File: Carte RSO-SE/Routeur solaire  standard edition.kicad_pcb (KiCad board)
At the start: 2 copper layers, 103.5 x 174.1 mm, 48 parts

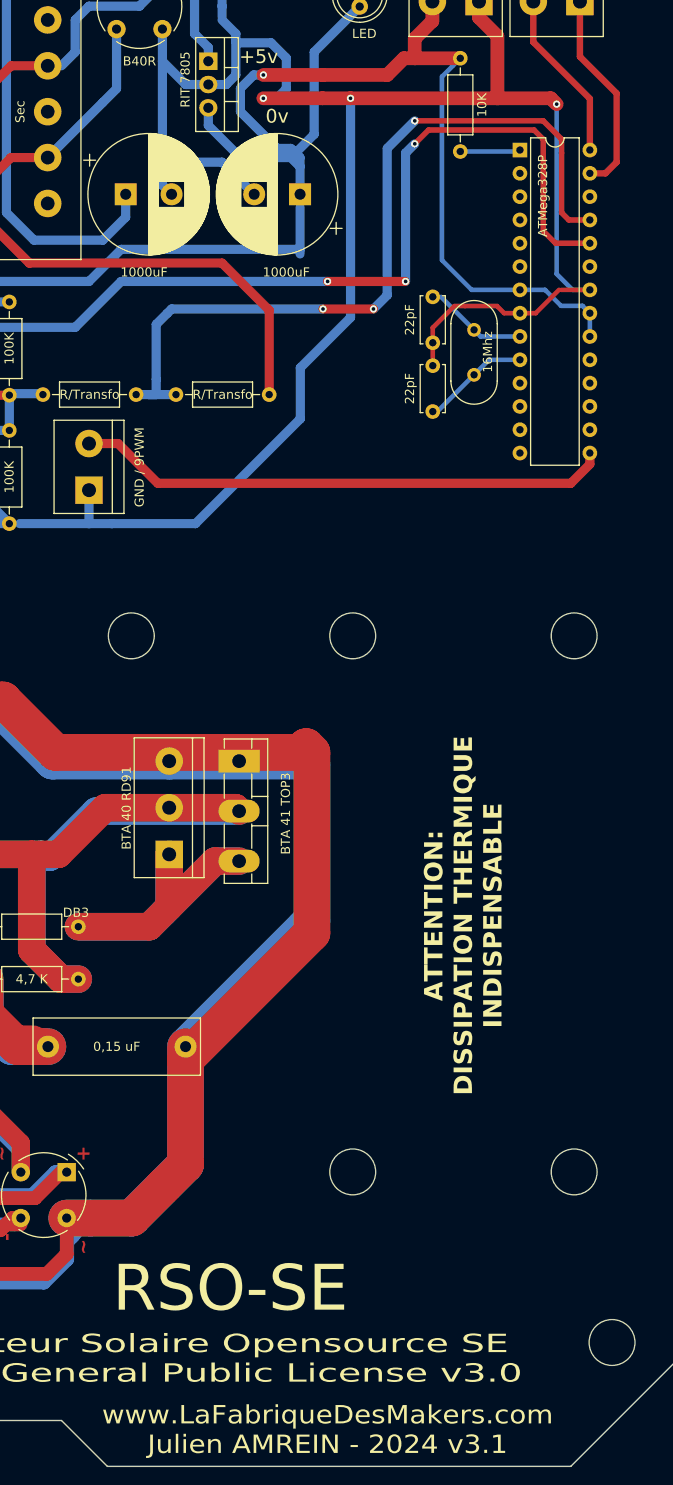
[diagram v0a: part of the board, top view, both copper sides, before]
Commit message: Ajout prise pour sonde de température en A3
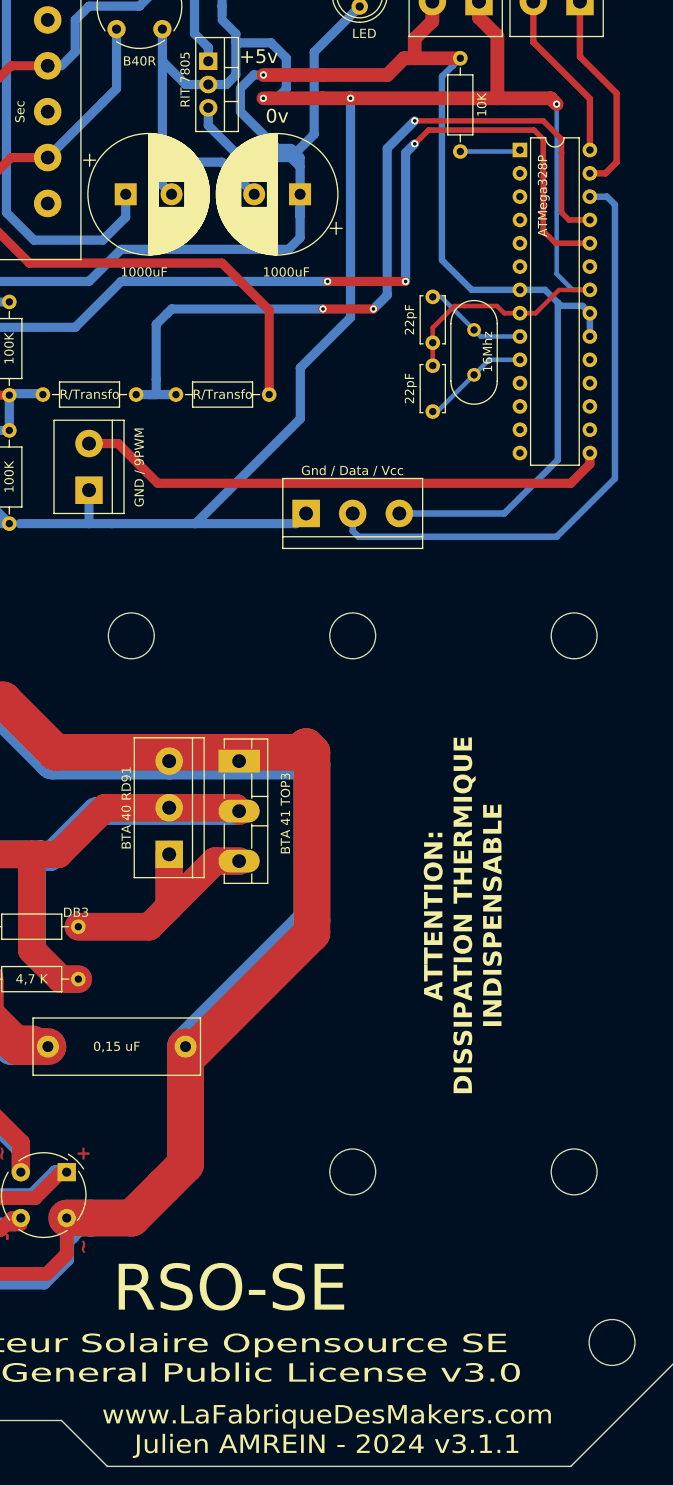
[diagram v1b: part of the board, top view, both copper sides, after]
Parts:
- added Gnd / Data / Vcc: TerminalBlock_bornier-3_P5.08mm, TerminalBlock:TerminalBlock_bornier-3_P5.08mm, F.Cu at (81.9, 87.0)
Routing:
- net (no net): track 2042.2 -> 2159.0 mm
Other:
- board text added: "www.LaFabriqueDesMakers.com Julien AMREIN - 2024 v3.1.1"
- board text removed: "www.LaFabriqueDesMakers.com Julien AMREIN - 2024 v3.1"

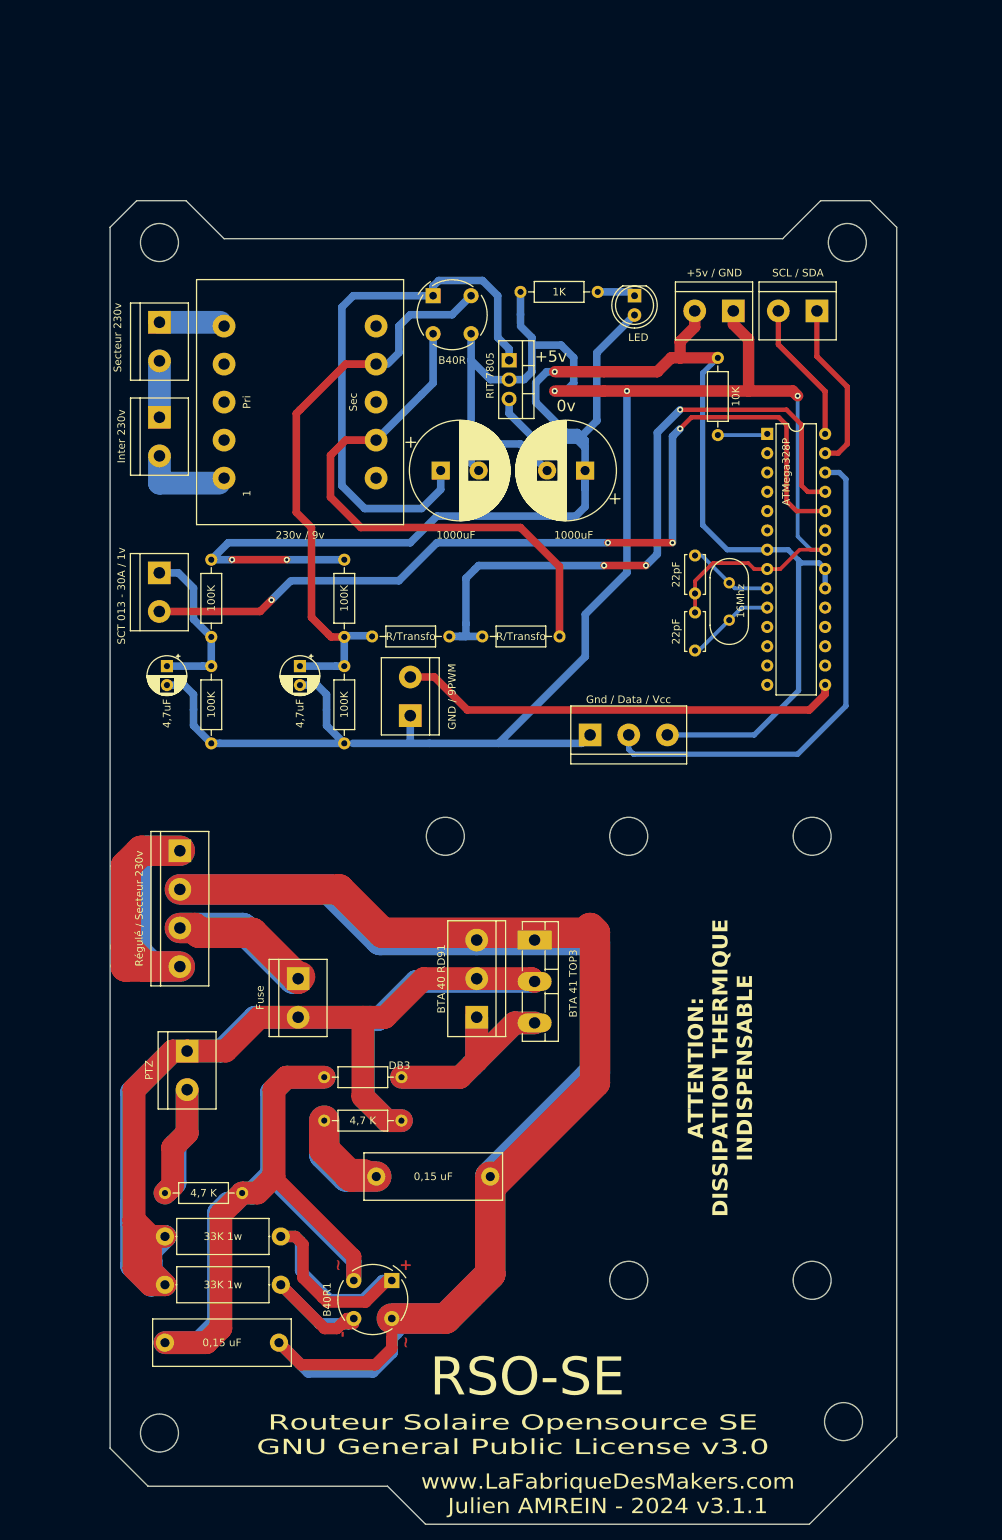
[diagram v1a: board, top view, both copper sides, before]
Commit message: Design de carte pour boitier intégré
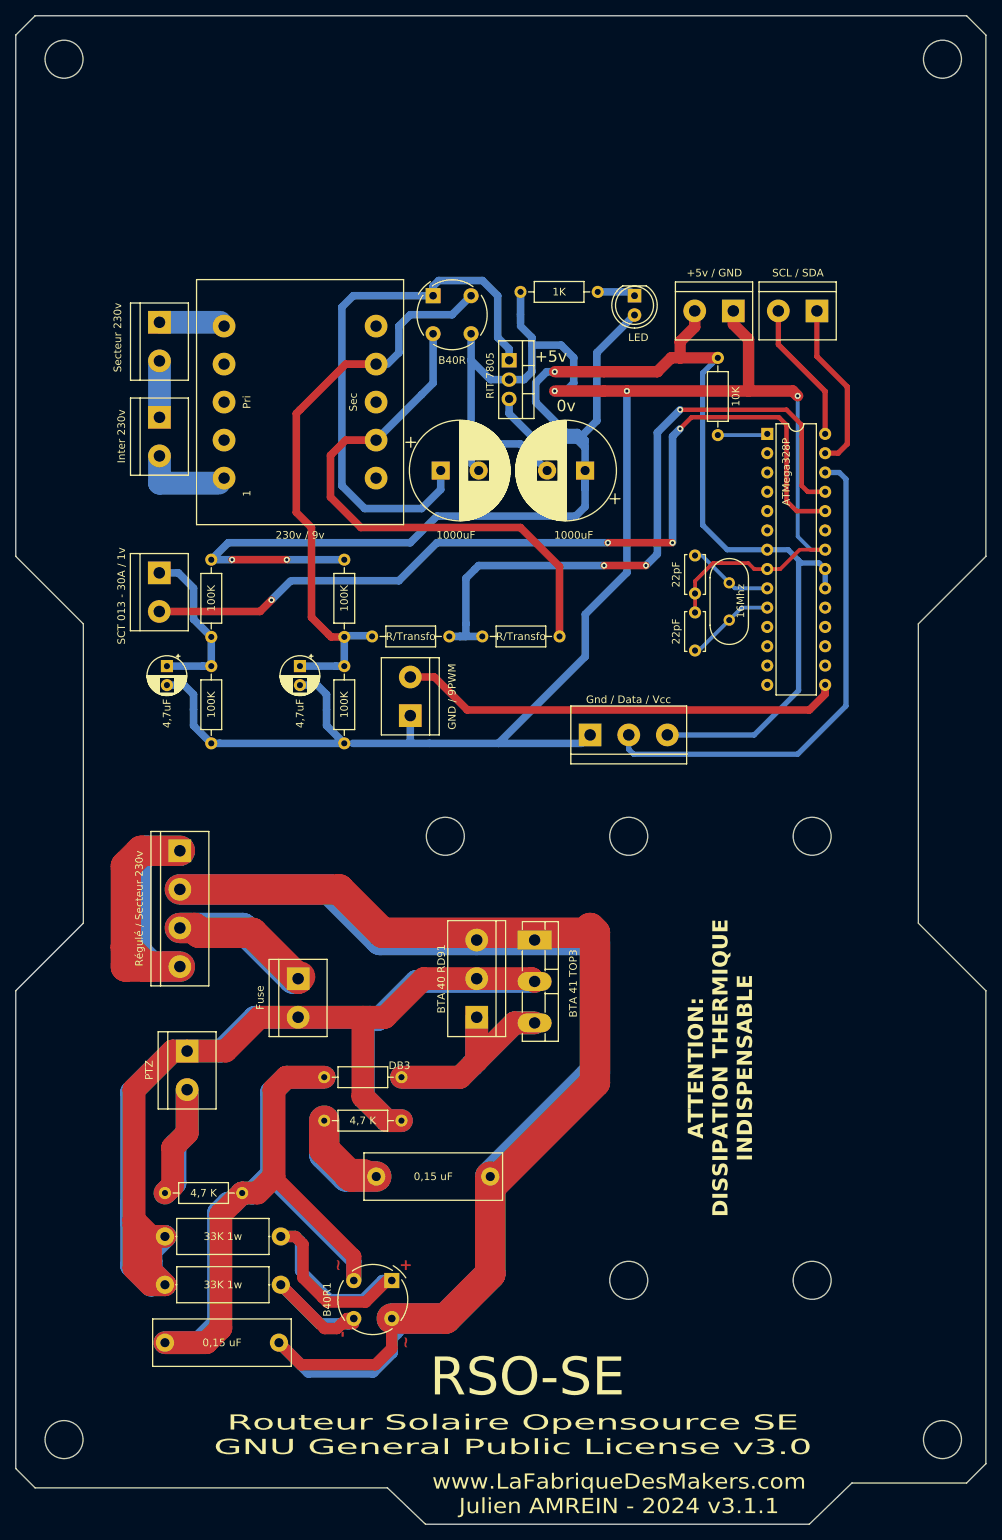
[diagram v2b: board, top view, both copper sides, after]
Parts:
- removed the ? at (115.8, 22.2)
- removed the ? at (25.3, 22.2)
- removed the ? at (25.3, 178.8)
- removed the ? at (115.3, 177.3)
- added ?: MountingHole_5mm, MountingHole:MountingHole_5mm, F.Cu at (128.3, 179.7)
- added ?: MountingHole_5mm, MountingHole:MountingHole_5mm, F.Cu at (12.7, -1.91)
- added ?: MountingHole_5mm, MountingHole:MountingHole_5mm, F.Cu at (128.3, -1.91)
- added ?: MountingHole_5mm, MountingHole:MountingHole_5mm, F.Cu at (12.7, 179.7)
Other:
- board size 103.5 x 174.1 mm -> 127.6 x 198.5 mm
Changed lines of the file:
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@@
   )
   (footprint "MountingHole:MountingHole_5mm" (layer "F.Cu")
-    (at 115.755 22.21)
+    (at 128.27 179.705)
     (descr "Mounting Hole 5mm, no annular")
     (tags "mounting hole 5mm no annular")
@@
       (stroke (width 0.05) (type solid)) (fill none) (layer "F.CrtYd"))
     (pad "" np_thru_hole circle (at 0 0) (size 5 5) (drill 5) (layers "*.Cu" "*.Mask"))
+    (pad "" np_thru_hole circle (at 0 0) (size 5 5) (drill 5) (layers "*.Cu" "*.Mask"))
   )
   (footprint "MountingHole:MountingHole_5mm" (layer "F.Cu")
-    (at 25.255 22.21)
+    (at 12.7 -1.905)
     (descr "Mounting Hole 5mm, no annular")
     (tags "mounting hole 5mm no annular")
@@
       (stroke (width 0.05) (type solid)) (fill none) (layer "F.CrtYd"))
     (pad "" np_thru_hole circle (at 0 0) (size 5 5) (drill 5) (layers "*.Cu" "*.Mask"))
-  )
-  (footprint "MountingHole:MountingHole_5mm" (layer "F.Cu")
-    (at 25.255 178.84)
-    (descr "Mounting Hole 5mm, no annular")
-    (tags "mounting hole 5mm no annular")
-    (attr exclude_from_pos_files exclude_from_bom)
-    (fp_text reference "" (at 0 -6) (layer "F.SilkS")
-        (effects (font (size 1 1) (thickness 0.15)))
-    )
-    (fp_text value "MountingHole_5mm" (at 0 6) (layer "F.Fab")
-        (effects (font (size 1 1) (thickness 0.15)))
-    )
-    (fp_text user "${REFERENCE}" (at 0.3 0) (layer "F.Fab")
-        (effects (font (size 1 1) (thickness 0.15)))
-    )
-    (fp_circle (center 0 0) (end 5 0)
-      (stroke (width 0.15) (type solid)) (fill none) (layer "Cmts.User"))
-    (fp_circle (center 0 0) (end 5.25 0)
-      (stroke (width 0.05) (type solid)) (fill none) (layer "F.CrtYd"))
-    (pad "" np_thru_hole circle (at 0 0) (size 5 5) (drill 5) (layers "*.Cu" "*.Mask"))
-  )
-  (footprint "MountingHole:MountingHole_5mm" (layer "F.Cu")
-    (at 115.255 177.34)
-    (descr "Mounting Hole 5mm, no annular")
-    (tags "mounting hole 5mm no annular")
-    (attr exclude_from_pos_files exclude_from_bom)
-    (fp_text reference "" (at 0 -6) (layer "F.SilkS")
-        (effects (font (size 1 1) (thickness 0.15)))
-    )
-    (fp_text value "MountingHole_5mm" (at 0 6) (layer "F.Fab")
-        (effects (font (size 1 1) (thickness 0.15)))
-    )
-    (fp_text user "${REFERENCE}" (at 0.3 0) (layer "F.Fab")
-        (effects (font (size 1 1) (thickness 0.15)))
-    )
-    (fp_circle (center 0 0) (end 5 0)
-      (stroke (width 0.15) (type solid)) (fill none) (layer "Cmts.User"))
-    (fp_circle (center 0 0) (end 5.25 0)
-      (stroke (width 0.05) (type solid)) (fill none) (layer "F.CrtYd"))
     (pad "" np_thru_hole circle (at 0 0) (size 5 5) (drill 5) (layers "*.Cu" "*.Mask"))
   )
@@
       (rotate (xyz 0 0 0))
     )
+  )
+  (footprint "MountingHole:MountingHole_5mm" (layer "F.Cu")
+    (at 128.27 -1.905)
+    (descr "Mounting Hole 5mm, no annular")
+    (tags "mounting hole 5mm no annular")
+    (attr exclude_from_pos_files exclude_from_bom)
+    (fp_text reference "" (at 0 -6) (layer "F.SilkS")
+        (effects (font (size 1 1) (thickness 0.15)))
+    )
+    (fp_text value "MountingHole_5mm" (at 0 6) (layer "F.Fab")
+        (effects (font (size 1 1) (thickness 0.15)))
+    )
+    (fp_text user "${REFERENCE}" (at 0.3 0) (layer "F.Fab")
+        (effects (font (size 1 1) (thickness 0.15)))
+    )
+    (fp_circle (center 0 0) (end 5 0)
+      (stroke (width 0.15) (type solid)) (fill none) (layer "Cmts.User"))
+    (fp_circle (center 0 0) (end 5.25 0)
+      (stroke (width 0.05) (type solid)) (fill none) (layer "F.CrtYd"))
+    (pad "" np_thru_hole circle (at 0 0) (size 5 5) (drill 5) (layers "*.Cu" "*.Mask"))
+    (pad "" np_thru_hole circle (at 0 0) (size 5 5) (drill 5) (layers "*.Cu" "*.Mask"))
   )
   (footprint "MountingHole:MountingHole_5mm" (layer "F.Cu")
@@
     )
   )
-  (gr_line (start 18.755 180.84) (end 18.755 20.21)
+  (footprint "MountingHole:MountingHole_5mm" (layer "F.Cu")
+    (at 12.7 179.705)
+    (descr "Mounting Hole 5mm, no annular")
+    (tags "mounting hole 5mm no annular")
+    (attr exclude_from_pos_files exclude_from_bom)
+    (fp_text reference "" (at 0 -6) (layer "F.SilkS")
+        (effects (font (size 1 1) (thickness 0.15)))
+    )
+    (fp_text value "MountingHole_5mm" (at 0 6) (layer "F.Fab")
+        (effects (font (size 1 1) (thickness 0.15)))
+    )
+    (fp_text user "${REFERENCE}" (at 0.3 0) (layer "F.Fab")
+        (effects (font (size 1 1) (thickness 0.15)))
+    )
+    (fp_circle (center 0 0) (end 5 0)
+      (stroke (width 0.15) (type solid)) (fill none) (layer "Cmts.User"))
+    (fp_circle (center 0 0) (end 5.25 0)
+      (stroke (width 0.05) (type solid)) (fill none) (layer "F.CrtYd"))
+    (pad "" np_thru_hole circle (at 0 0) (size 5 5) (drill 5) (layers "*.Cu" "*.Mask"))
+    (pad "" np_thru_hole circle (at 0 0) (size 5 5) (drill 5) (layers "*.Cu" "*.Mask"))
+  )
+  (gr_line (start 110.755 190.84) (end 116.355 185.42)
     (stroke (width 0.15) (type solid)) (layer "Edge.Cuts"))
-  (gr_line (start 110.755 190.84) (end 122.255 179.34)
+  (gr_line (start 60.255 190.84) (end 55.255 186.055)
     (stroke (width 0.15) (type solid)) (layer "Edge.Cuts"))
-  (gr_line (start 60.255 190.84) (end 55.255 185.84)
+  (gr_line (start 55.255 186.055) (end 8.89 186.055)
     (stroke (width 0.15) (type solid)) (layer "Edge.Cuts"))
-  (gr_line (start 55.255 185.84) (end 23.755 185.84)
+  (gr_line (start 6.35 120.65) (end 6.35 183.515)
     (stroke (width 0.15) (type solid)) (layer "Edge.Cuts"))
-  (gr_line (start 23.755 185.84) (end 18.755 180.84)
+  (gr_line (start 133.985 -5.08) (end 131.445 -7.62)
+    (stroke (width 0.15) (type default)) (layer "Edge.Cuts"))
+  (gr_line (start 133.985 120.65) (end 125.095 111.76)
+    (stroke (width 0.15) (type default)) (layer "Edge.Cuts"))
+  (gr_line (start 133.985 182.88) (end 131.445 185.42)
+    (stroke (width 0.15) (type default)) (layer "Edge.Cuts"))
+  (gr_line (start 133.985 120.65) (end 133.985 182.88)
     (stroke (width 0.15) (type solid)) (layer "Edge.Cuts"))
-  (gr_line (start 33.755 21.71) (end 28.755 16.71)
+  (gr_line (start 6.35 183.515) (end 8.89 186.055)
+    (stroke (width 0.15) (type default)) (layer "Edge.Cuts"))
+  (gr_line (start 15.24 111.76) (end 6.35 120.65)
+    (stroke (width 0.15) (type default)) (layer "Edge.Cuts"))
+  (gr_line (start 15.24 72.39) (end 6.35 63.5)
+    (stroke (width 0.15) (type default)) (layer "Edge.Cuts"))
+  (gr_line (start 125.095 72.39) (end 125.095 111.76)
     (stroke (width 0.15) (type solid)) (layer "Edge.Cuts"))
-  (gr_line (start 112.255 16.71) (end 107.255 21.71)
+  (gr_line (start 133.985 63.5) (end 125.095 72.39)
+    (stroke (width 0.15) (type default)) (layer "Edge.Cuts"))
+  (gr_line (start 133.985 -5.08) (end 133.985 63.5)
     (stroke (width 0.15) (type solid)) (layer "Edge.Cuts"))
-  (gr_line (start 112.255 16.71) (end 118.755 16.71)
-    (stroke (width 0.15) (type solid)) (layer "Edge.Cuts"))
-  (gr_line (start 22.255 16.71) (end 28.755 16.71)
-    (stroke (width 0.15) (type solid)) (layer "Edge.Cuts"))
-  (gr_line (start 22.255 16.71) (end 18.755 20.21)
-    (stroke (width 0.15) (type solid)) (layer "Edge.Cuts"))
-  (gr_line (start 118.755 16.71) (end 122.255 20.21)
-    (stroke (width 0.15) (type solid)) (layer "Edge.Cuts"))
-  (gr_line (start 122.255 20.21) (end 122.255 179.34)
+  (gr_line (start 6.35 -5.08) (end 8.89 -7.62)
+    (stroke (width 0.15) (type default)) (layer "Edge.Cuts"))
+  (gr_line (start 15.24 72.39) (end 15.24 111.76)
+    (stroke (width 0.15) (type default)) (layer "Edge.Cuts"))
+  (gr_line (start 6.35 -5.08) (end 6.35 63.5)
     (stroke (width 0.15) (type solid)) (layer "Edge.Cuts"))
   (gr_line (start 110.755 190.84) (end 60.255 190.84)
     (stroke (width 0.15) (type solid)) (layer "Edge.Cuts"))
-  (gr_line (start 33.755 21.71) (end 107.255 21.71)
-    (stroke (width 0.15) (type solid)) (layer "Edge.Cuts"))
+  (gr_line (start 131.445 -7.62) (end 8.89 -7.62)
+    (stroke (width 0.15) (type default)) (layer "Edge.Cuts"))
+  (gr_line (start 131.445 185.42) (end 116.355 185.42)
+    (stroke (width 0.15) (type default)) (layer "Edge.Cuts"))
   (gr_text "+" (at 56.8325 155.8925 -90) (layer "F.Cu")
     (effects (font (size 1.5 1.5) (thickness 0.3) bold) (justify left bottom))
@@
   )
   (gr_text "Routeur Solaire Opensource SE\nGNU General Public License v3.0" (at 71.755 179.07) (layer "F.SilkS")
-    (effects (font (size 2 3) (thickness 0.25)))
+    (effects (font (size 2 3.5) (thickness 0.25)))
   )
   (gr_text "+5v" (at 76.755 37.21) (layer "F.SilkS")
@@
     (effects (font (size 5 5) (thickness 1)))
   )
-  (gr_text "www.LaFabriqueDesMakers.com\nJulien AMREIN - 2024 v3.1.1" (at 84.255 186.84) (layer "F.SilkS")
+  (gr_text "www.LaFabriqueDesMakers.com\nJulien AMREIN - 2024 v3.1.1" (at 85.725 186.84) (layer "F.SilkS")
     (effects (font (size 2 2.2) (thickness 0.25)))
   )

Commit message: Ajout de l'alimentation unique puissance - commande
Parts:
- moved 0,15 uF 140.6 mm to (-86.6, 154.0)
- moved 0,15 uF 140.6 mm to (-114.4, 175.8)
- moved 33K 1w 140.6 mm to (-114.4, 168.2)
- moved 33K 1w 140.6 mm to (-114.4, 161.9)
- moved 4,7 K 140.6 mm to (-93.4, 146.6)
- moved 4,7 K 140.6 mm to (-114.4, 156.2)
- moved ? 140.6 mm to (-12.1, 188.6)
- moved ? 140.6 mm to (-127.6, 6.99)
- moved ? 140.6 mm to (-29.2, 109.2)
- moved ? 140.6 mm to (-12.1, 6.99)
- moved ? 140.6 mm to (-77.5, 109.2)
- moved ? 140.6 mm to (-29.2, 167.6)
- moved ? 140.6 mm to (-53.3, 167.6)
- moved ? 140.6 mm to (-53.3, 109.2)
- moved ? 140.6 mm to (-127.6, 188.6)
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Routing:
- net (no net): track 2159.0 -> 2323.2 mm

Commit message: Ajout trous écran LCD
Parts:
- added ?: MountingHole_5mm, MountingHole:MountingHole_5mm, F.Cu at (-106.7, 1.27)
- added ?: MountingHole_5mm, MountingHole:MountingHole_5mm, F.Cu at (-53.3, -114.9)
- added ?: MountingHole_5mm, MountingHole:MountingHole_5mm, F.Cu at (-53.3, -83.8)
- added ?: MountingHole_5mm, MountingHole:MountingHole_5mm, F.Cu at (-31.8, 1.27)
- added ?: MountingHole_5mm, MountingHole:MountingHole_5mm, F.Cu at (-31.8, 32.4)
- added ?: MountingHole_5mm, MountingHole:MountingHole_5mm, F.Cu at (-106.7, 32.4)
- added ?: MountingHole_5mm, MountingHole:MountingHole_5mm, F.Cu at (-128.3, -114.9)
- added ?: MountingHole_5mm, MountingHole:MountingHole_5mm, F.Cu at (-128.3, -83.8)
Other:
- board size 127.6 x 198.5 mm -> 127.6 x 203.2 mm
